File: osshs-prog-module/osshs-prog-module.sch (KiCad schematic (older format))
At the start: 7 parts, among them J1 Conn_02x03_Odd_Even, SW1 SW_Push, U1 STM32F103RETx

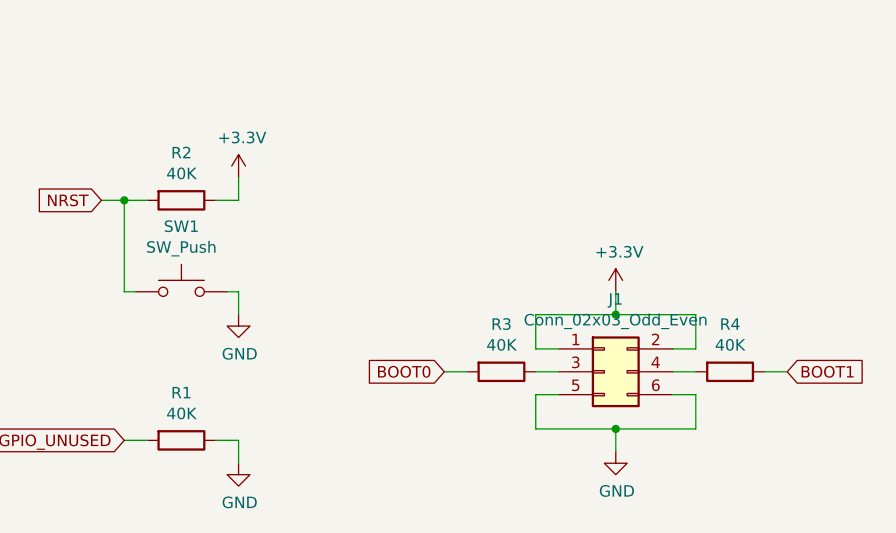
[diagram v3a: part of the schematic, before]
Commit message: Change 40k resistors to 39k
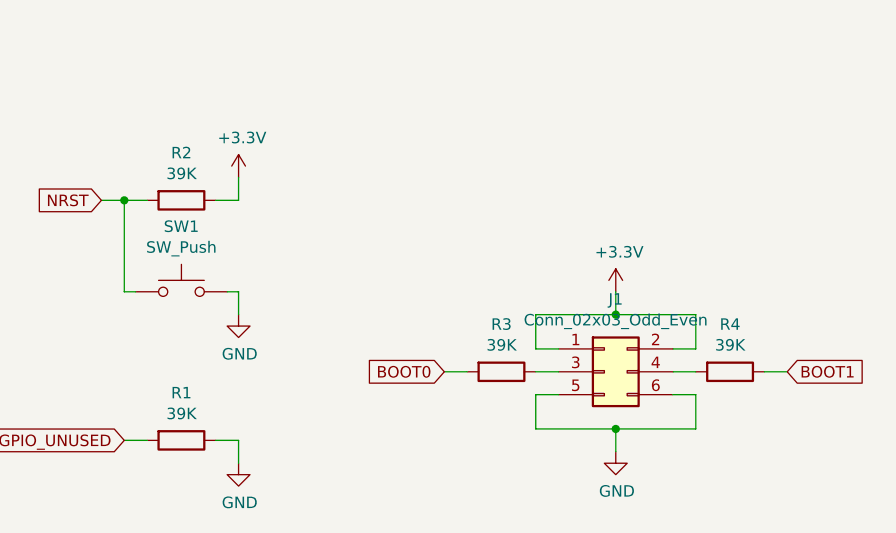
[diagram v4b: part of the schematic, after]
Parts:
- R1, R2, R3, R4: value 40K -> 39K
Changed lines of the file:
@@
 EESchema Schematic File Version 4
-LIBS:osshs-prog-module-cache
 EELAYER 30 0
 EELAYER END
@@
 P 1350 7450
 F 0 "R1" V 1143 7450 50  0000 C CNN
-F 1 "40K" V 1234 7450 50  0000 C CNN
+F 1 "39K" V 1234 7450 50  0000 C CNN
 F 2 "Resistor_SMD:R_0805_2012Metric" V 1280 7450 50  0001 C CNN
 F 3 "~" H 1350 7450 50  0001 C CNN
@@
 P 1350 6400
 F 0 "R2" V 1143 6400 50  0000 C CNN
-F 1 "40K" V 1234 6400 50  0000 C CNN
+F 1 "39K" V 1234 6400 50  0000 C CNN
 F 2 "Resistor_SMD:R_0805_2012Metric" V 1280 6400 50  0001 C CNN
 F 3 "~" H 1350 6400 50  0001 C CNN
@@
 	1    0    0    -1
 $EndComp
-$Comp
-L Device:R R3
-U 1 1 5DEDABE6
-P 2750 7150
-F 0 "R3" V 2543 7150 50  0000 C CNN
-F 1 "40K" V 2634 7150 50  0000 C CNN
-F 2 "Resistor_SMD:R_0805_2012Metric" V 2680 7150 50  0001 C CNN
-F 3 "~" H 2750 7150 50  0001 C CNN
-	1    2750 7150
-	0    1    1    0
-$EndComp
-$Comp
-L Device:R R4
-U 1 1 5DEDE2CE
-P 3750 7150
-F 0 "R4" V 3543 7150 50  0000 C CNN
-F 1 "40K" V 3634 7150 50  0000 C CNN
-F 2 "Resistor_SMD:R_0805_2012Metric" V 3680 7150 50  0001 C CNN
-F 3 "~" H 3750 7150 50  0001 C CNN
-	1    3750 7150
-	0    1    1    0
-$EndComp
 Wire Wire Line
 	3500 7150 3600 7150
@@
 Text GLabel 4000 7150 2    50   Input ~ 0
 BOOT1
+$Comp
+L Device:R R4
+U 1 1 5DEDE2CE
+P 3750 7150
+F 0 "R4" V 3543 7150 50  0000 C CNN
+F 1 "39K" V 3634 7150 50  0000 C CNN
+F 2 "Resistor_SMD:R_0805_2012Metric" V 3680 7150 50  0001 C CNN
+F 3 "~" H 3750 7150 50  0001 C CNN
+	1    3750 7150
+	0    1    1    0
+$EndComp
+$Comp
+L Device:R R3
+U 1 1 5DEDABE6
+P 2750 7150
+F 0 "R3" V 2543 7150 50  0000 C CNN
+F 1 "39K" V 2634 7150 50  0000 C CNN
+F 2 "Resistor_SMD:R_0805_2012Metric" V 2680 7150 50  0001 C CNN
+F 3 "~" H 2750 7150 50  0001 C CNN
+	1    2750 7150
+	0    1    1    0
+$EndComp
 $EndSCHEMATC

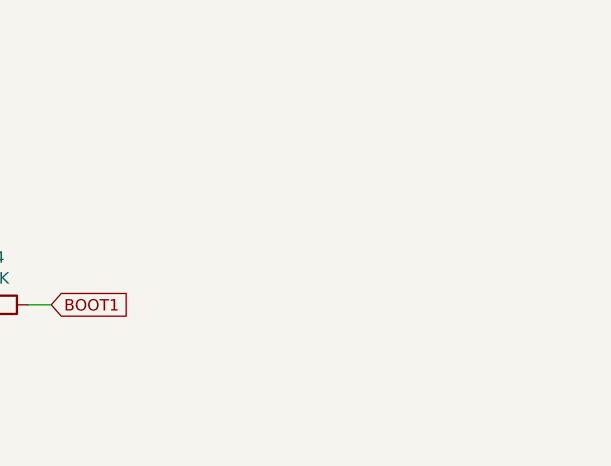
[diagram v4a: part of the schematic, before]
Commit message: Add power and status LED indicators
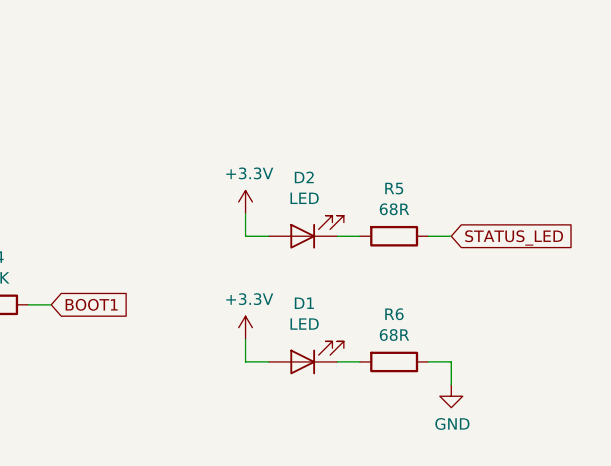
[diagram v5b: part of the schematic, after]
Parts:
- added D1, D2: LED, LED_SMD:LED_0805_2012Metric, symbol Device:LED
- added R5, R6: 68R, Resistor_SMD:R_0805_2012Metric, symbol Device:R
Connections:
- net +3V3: now also D1.2 (A), D2.2 (A)
- net GND: now also R6.1
- new net: D2.1 (K), R5.2
- new net: D1.1 (K), R6.2
- new net STATUS_LED: R5.1
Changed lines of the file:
@@
 	0    1    1    0
 $EndComp
+$Comp
+L Device:R R5
+U 1 1 5E01210D
+P 5500 6850
+F 0 "R5" V 5293 6850 50  0000 C CNN
+F 1 "68R" V 5384 6850 50  0000 C CNN
+F 2 "Resistor_SMD:R_0805_2012Metric" V 5430 6850 50  0001 C CNN
+F 3 "~" H 5500 6850 50  0001 C CNN
+	1    5500 6850
+	0    1    1    0
+$EndComp
+$Comp
+L Device:LED D2
+U 1 1 5E04B9FB
+P 5100 6850
+F 0 "D2" H 5093 6595 50  0000 C CNN
+F 1 "LED" H 5093 6686 50  0000 C CNN
+F 2 "LED_SMD:LED_0805_2012Metric" H 5100 6850 50  0001 C CNN
+F 3 "~" H 5100 6850 50  0001 C CNN
+	1    5100 6850
+	-1   0    0    1
+$EndComp
+Wire Wire Line
+	5250 6850 5350 6850
+Wire Wire Line
+	4850 6850 4850 6750
+$Comp
+L power:+3.3V #PWR0108
+U 1 1 5E05712B
+P 4850 6750
+F 0 "#PWR0108" H 4850 6600 50  0001 C CNN
+F 1 "+3.3V" H 4865 6923 50  0000 C CNN
+F 2 "" H 4850 6750 50  0001 C CNN
+F 3 "" H 4850 6750 50  0001 C CNN
+	1    4850 6750
+	1    0    0    -1
+$EndComp
+Wire Wire Line
+	4850 6850 4950 6850
+Wire Wire Line
+	5650 6850 5750 6850
+Text GLabel 5750 6850 2    50   Input ~ 0
+STATUS_LED
+$Comp
+L Device:LED D1
+U 1 1 5E070339
+P 5100 7400
+F 0 "D1" H 5093 7145 50  0000 C CNN
+F 1 "LED" H 5093 7236 50  0000 C CNN
+F 2 "LED_SMD:LED_0805_2012Metric" H 5100 7400 50  0001 C CNN
+F 3 "~" H 5100 7400 50  0001 C CNN
+	1    5100 7400
+	-1   0    0    1
+$EndComp
+Wire Wire Line
+	4850 7400 4850 7300
+$Comp
+L power:+3.3V #PWR0109
+U 1 1 5E070341
+P 4850 7300
+F 0 "#PWR0109" H 4850 7150 50  0001 C CNN
+F 1 "+3.3V" H 4865 7473 50  0000 C CNN
+F 2 "" H 4850 7300 50  0001 C CNN
+F 3 "" H 4850 7300 50  0001 C CNN
+	1    4850 7300
+	1    0    0    -1
+$EndComp
+Wire Wire Line
+	4850 7400 4950 7400
+$Comp
+L Device:R R6
+U 1 1 5E07DB97
+P 5500 7400
+F 0 "R6" V 5293 7400 50  0000 C CNN
+F 1 "68R" V 5384 7400 50  0000 C CNN
+F 2 "Resistor_SMD:R_0805_2012Metric" V 5430 7400 50  0001 C CNN
+F 3 "~" H 5500 7400 50  0001 C CNN
+	1    5500 7400
+	0    1    1    0
+$EndComp
+Wire Wire Line
+	5250 7400 5350 7400
+Wire Wire Line
+	5750 7400 5750 7500
+$Comp
+L power:GND #PWR0110
+U 1 1 5E099AA7
+P 5750 7500
+F 0 "#PWR0110" H 5750 7250 50  0001 C CNN
+F 1 "GND" H 5755 7327 50  0000 C CNN
+F 2 "" H 5750 7500 50  0001 C CNN
+F 3 "" H 5750 7500 50  0001 C CNN
+	1    5750 7500
+	1    0    0    -1
+$EndComp
+Wire Wire Line
+	5650 7400 5750 7400
 $EndSCHEMATC

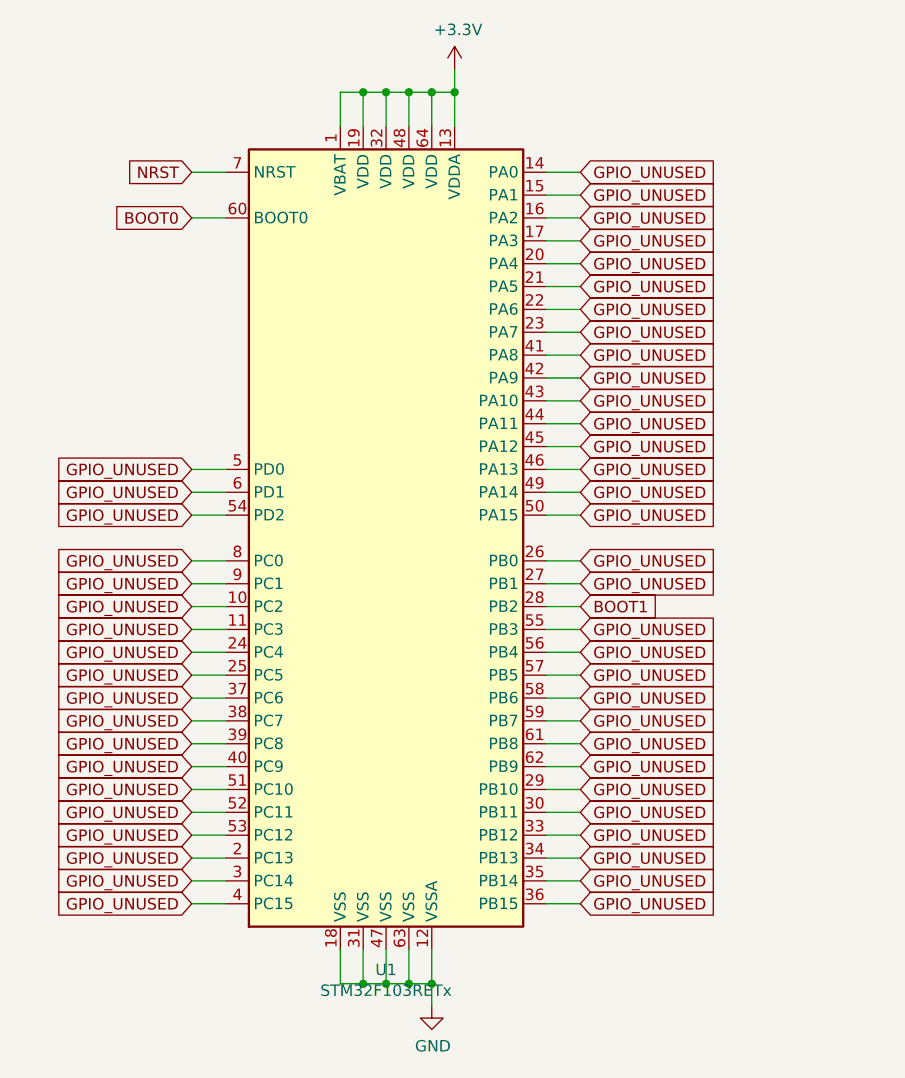
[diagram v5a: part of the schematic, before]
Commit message: Handle floating GPIO's in firmware
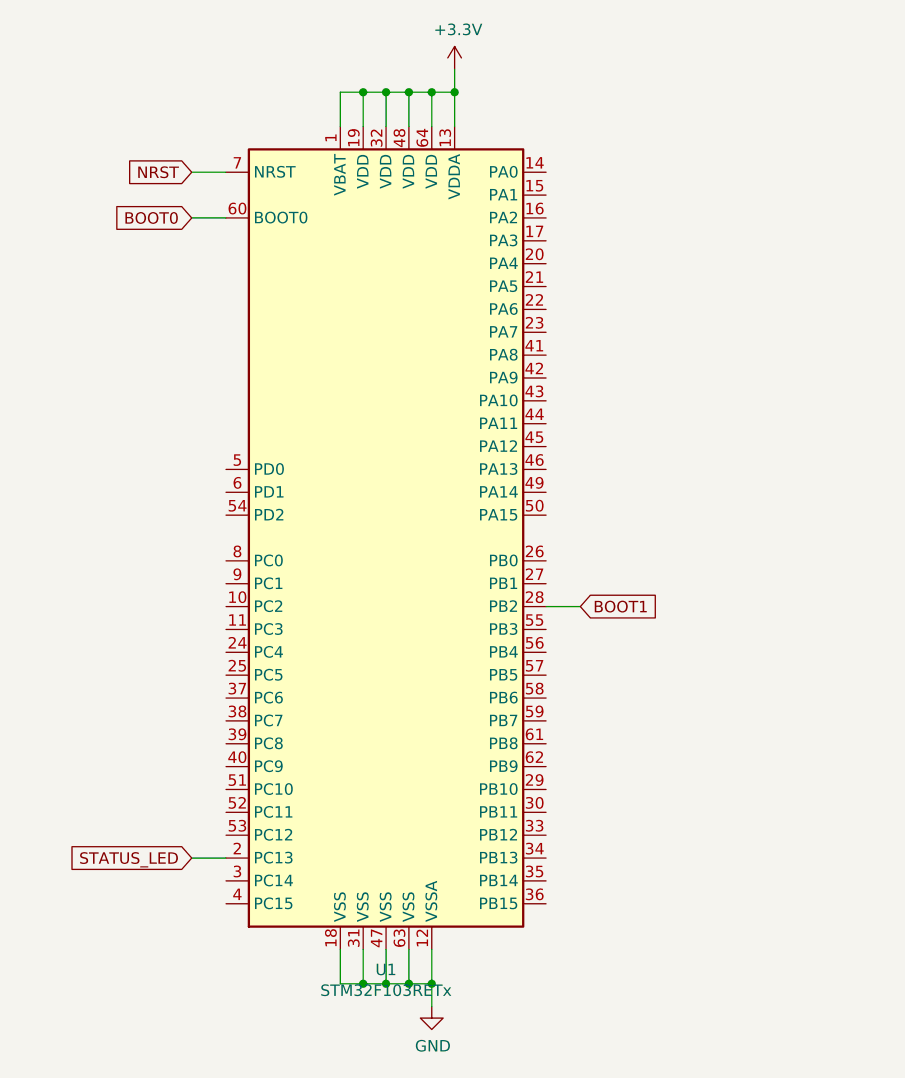
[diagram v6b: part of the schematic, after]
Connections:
- net GPIO_UNUSED: no longer U1.10 (PC2), U1.11 (PC3), U1.14 (PA0), U1.15 (PA1), U1.16 (PA2), U1.17 (PA3), U1.2 (PC13), U1.20 (PA4), U1.21 (PA5), U1.22 (PA6), U1.23 (PA7), U1.24 (PC4), U1.25 (PC5), U1.26 (PB0), U1.27 (PB1), U1.29 (PB10), U1.3 (PC14), U1.30 (PB11), U1.33 (PB12), U1.34 (PB13), U1.35 (PB14), U1.36 (PB15), U1.37 (PC6), U1.38 (PC7), U1.39 (PC8), U1.4 (PC15), U1.40 (PC9), U1.41 (PA8), U1.42 (PA9), U1.43 (PA10), U1.44 (PA11), U1.45 (PA12), U1.46 (PA13), U1.49 (PA14), U1.5 (PD0), U1.50 (PA15), U1.51 (PC10), U1.52 (PC11), U1.53 (PC12), U1.54 (PD2), U1.55 (PB3), U1.56 (PB4), U1.57 (PB5), U1.58 (PB6), U1.59 (PB7), U1.6 (PD1), U1.61 (PB8), U1.62 (PB9), U1.8 (PC0), U1.9 (PC1)
- net STATUS_LED: now also U1.2 (PC13)
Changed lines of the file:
@@
 	1300 1400 1150 1400
 Wire Wire Line
-	1300 2500 1150 2500
-Wire Wire Line
-	1300 2600 1150 2600
-Wire Wire Line
-	1300 2700 1150 2700
-Wire Wire Line
-	1300 2900 1150 2900
-Wire Wire Line
-	1300 3000 1150 3000
-Wire Wire Line
-	1300 3100 1150 3100
-Wire Wire Line
-	1300 3200 1150 3200
-Wire Wire Line
-	1300 3300 1150 3300
-Wire Wire Line
-	1300 3400 1150 3400
-Wire Wire Line
-	1300 3500 1150 3500
-Wire Wire Line
-	1300 3600 1150 3600
-Wire Wire Line
-	1300 3700 1150 3700
-Wire Wire Line
-	1300 3800 1150 3800
-Wire Wire Line
-	1300 3900 1150 3900
-Wire Wire Line
-	1300 4000 1150 4000
-Wire Wire Line
-	1300 4100 1150 4100
-Wire Wire Line
 	1300 4200 1150 4200
-Wire Wire Line
-	1300 4300 1150 4300
-Wire Wire Line
-	1300 4400 1150 4400
 Wire Wire Line
 	1800 4600 1800 4750
@@
 	2200 4600 2200 4750
 Wire Wire Line
-	2700 4400 2850 4400
-Wire Wire Line
-	2700 4300 2850 4300
-Wire Wire Line
-	2700 4200 2850 4200
-Wire Wire Line
-	2700 4100 2850 4100
-Wire Wire Line
-	2700 4000 2850 4000
-Wire Wire Line
-	2700 3900 2850 3900
-Wire Wire Line
-	2700 3800 2850 3800
-Wire Wire Line
-	2700 3700 2850 3700
-Wire Wire Line
-	2700 3600 2850 3600
-Wire Wire Line
-	2700 3500 2850 3500
-Wire Wire Line
-	2700 3400 2850 3400
-Wire Wire Line
-	2700 3300 2850 3300
-Wire Wire Line
-	2700 3200 2850 3200
-Wire Wire Line
 	2700 3100 2850 3100
-Wire Wire Line
-	2700 3000 2850 3000
-Wire Wire Line
-	2700 2900 2850 2900
-Wire Wire Line
-	2700 2700 2850 2700
-Wire Wire Line
-	2700 2600 2850 2600
-Wire Wire Line
-	2700 2500 2850 2500
-Wire Wire Line
-	2700 2400 2850 2400
-Wire Wire Line
-	2700 2300 2850 2300
-Wire Wire Line
-	2700 2200 2850 2200
-Wire Wire Line
-	2700 2100 2850 2100
-Wire Wire Line
-	2700 2000 2850 2000
-Wire Wire Line
-	2700 1900 2850 1900
-Wire Wire Line
-	2700 1800 2850 1800
-Wire Wire Line
-	2700 1700 2850 1700
-Wire Wire Line
-	2700 1600 2850 1600
-Wire Wire Line
-	2700 1500 2850 1500
-Wire Wire Line
-	2700 1400 2850 1400
-Wire Wire Line
-	2700 1300 2850 1300
-Wire Wire Line
-	2700 1200 2850 1200
 Wire Wire Line
 	2300 1000 2300 850
@@
 Wire Wire Line
 	1800 1000 1800 850
-Text GLabel 2850 1200 2    50   Input ~ 0
-GPIO_UNUSED
-Text GLabel 2850 1300 2    50   Input ~ 0
-GPIO_UNUSED
-Text GLabel 2850 1400 2    50   Input ~ 0
-GPIO_UNUSED
-Text GLabel 2850 1500 2    50   Input ~ 0
-GPIO_UNUSED
-Text GLabel 2850 1600 2    50   Input ~ 0
-GPIO_UNUSED
-Text GLabel 2850 1700 2    50   Input ~ 0
-GPIO_UNUSED
-Text GLabel 2850 1800 2    50   Input ~ 0
-GPIO_UNUSED
-Text GLabel 2850 1900 2    50   Input ~ 0
-GPIO_UNUSED
-Text GLabel 2850 2000 2    50   Input ~ 0
-GPIO_UNUSED
-Text GLabel 2850 2100 2    50   Input ~ 0
-GPIO_UNUSED
-Text GLabel 2850 2200 2    50   Input ~ 0
-GPIO_UNUSED
-Text GLabel 2850 2300 2    50   Input ~ 0
-GPIO_UNUSED
-Text GLabel 2850 2400 2    50   Input ~ 0
-GPIO_UNUSED
-Text GLabel 2850 2500 2    50   Input ~ 0
-GPIO_UNUSED
-Text GLabel 2850 2600 2    50   Input ~ 0
-GPIO_UNUSED
-Text GLabel 2850 2700 2    50   Input ~ 0
-GPIO_UNUSED
-Text GLabel 2850 2900 2    50   Input ~ 0
-GPIO_UNUSED
-Text GLabel 2850 3000 2    50   Input ~ 0
-GPIO_UNUSED
 Text GLabel 2850 3100 2    50   Input ~ 0
 BOOT1
-Text GLabel 2850 3200 2    50   Input ~ 0
-GPIO_UNUSED
-Text GLabel 2850 3300 2    50   Input ~ 0
-GPIO_UNUSED
-Text GLabel 2850 3400 2    50   Input ~ 0
-GPIO_UNUSED
-Text GLabel 2850 3500 2    50   Input ~ 0
-GPIO_UNUSED
-Text GLabel 2850 3600 2    50   Input ~ 0
-GPIO_UNUSED
-Text GLabel 2850 3700 2    50   Input ~ 0
-GPIO_UNUSED
-Text GLabel 2850 3800 2    50   Input ~ 0
-GPIO_UNUSED
-Text GLabel 2850 3900 2    50   Input ~ 0
-GPIO_UNUSED
-Text GLabel 2850 4000 2    50   Input ~ 0
-GPIO_UNUSED
-Text GLabel 2850 4100 2    50   Input ~ 0
-GPIO_UNUSED
-Text GLabel 2850 4200 2    50   Input ~ 0
-GPIO_UNUSED
-Text GLabel 2850 4300 2    50   Input ~ 0
-GPIO_UNUSED
-Text GLabel 2850 4400 2    50   Input ~ 0
-GPIO_UNUSED
-Text GLabel 1150 4400 0    50   Input ~ 0
-GPIO_UNUSED
-Text GLabel 1150 4300 0    50   Input ~ 0
-GPIO_UNUSED
 Text GLabel 1150 4200 0    50   Input ~ 0
-GPIO_UNUSED
-Text GLabel 1150 4100 0    50   Input ~ 0
-GPIO_UNUSED
-Text GLabel 1150 3900 0    50   Input ~ 0
-GPIO_UNUSED
-Text GLabel 1150 4000 0    50   Input ~ 0
-GPIO_UNUSED
-Text GLabel 1150 3800 0    50   Input ~ 0
-GPIO_UNUSED
-Text GLabel 1150 3700 0    50   Input ~ 0
-GPIO_UNUSED
-Text GLabel 1150 3600 0    50   Input ~ 0
-GPIO_UNUSED
-Text GLabel 1150 3500 0    50   Input ~ 0
-GPIO_UNUSED
-Text GLabel 1150 3400 0    50   Input ~ 0
-GPIO_UNUSED
-Text GLabel 1150 3300 0    50   Input ~ 0
-GPIO_UNUSED
-Text GLabel 1150 3200 0    50   Input ~ 0
-GPIO_UNUSED
-Text GLabel 1150 3100 0    50   Input ~ 0
-GPIO_UNUSED
-Text GLabel 1150 3000 0    50   Input ~ 0
-GPIO_UNUSED
-Text GLabel 1150 2900 0    50   Input ~ 0
-GPIO_UNUSED
-Text GLabel 1150 2700 0    50   Input ~ 0
-GPIO_UNUSED
-Text GLabel 1150 2600 0    50   Input ~ 0
-GPIO_UNUSED
-Text GLabel 1150 2500 0    50   Input ~ 0
-GPIO_UNUSED
+STATUS_LED
 Text GLabel 1100 7450 0    50   Input ~ 0
 GPIO_UNUSED
